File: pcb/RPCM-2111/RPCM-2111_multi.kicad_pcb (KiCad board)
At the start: 2 copper layers, 79.8 x 96.9 mm, 84 parts, among them J1 Conn_01x04_Female, J2 Conn_01x04_Female, J3 Conn_01x08_Female, J4 Conn_01x08_Female, J5 Conn_01x04_Female, J6 Conn_01x05_Female, J7 Conn_01x03_Female, J8 Conn_01x04_Female

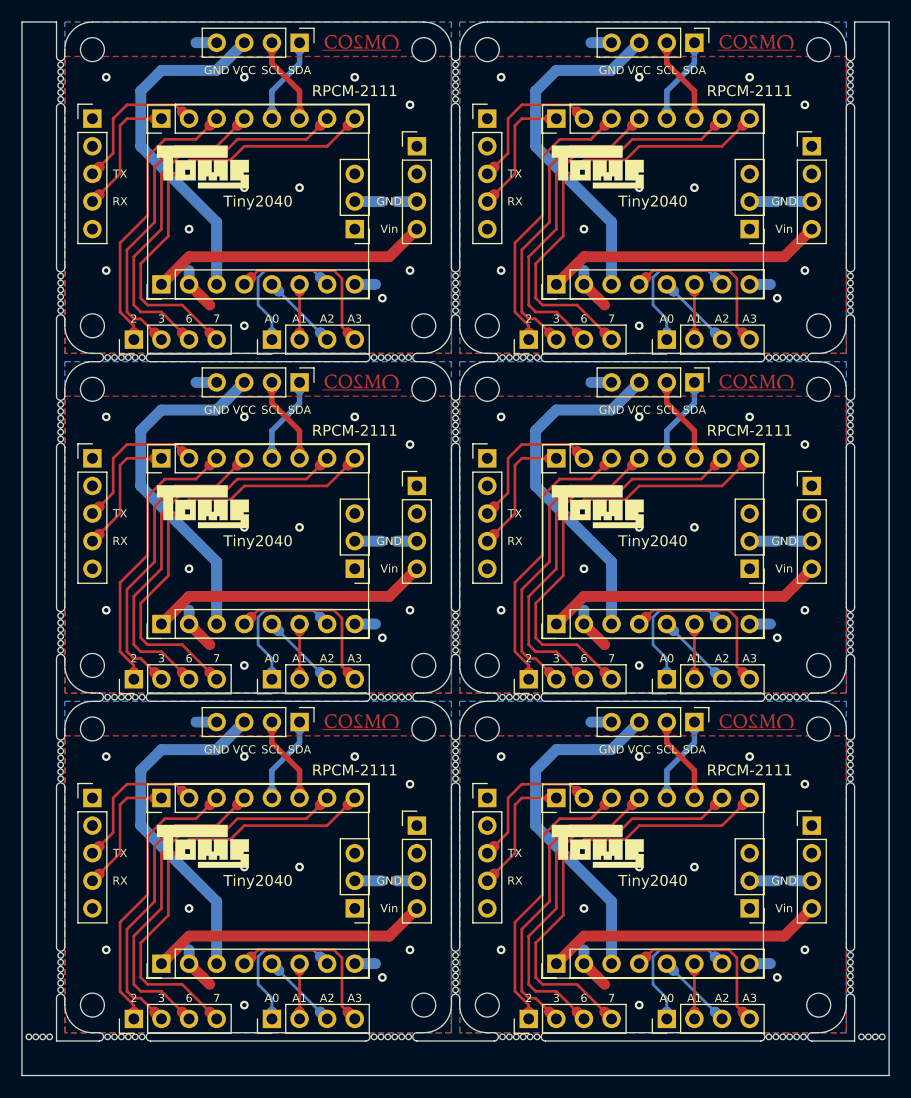
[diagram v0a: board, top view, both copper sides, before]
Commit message: :sparkles: fix to panelize
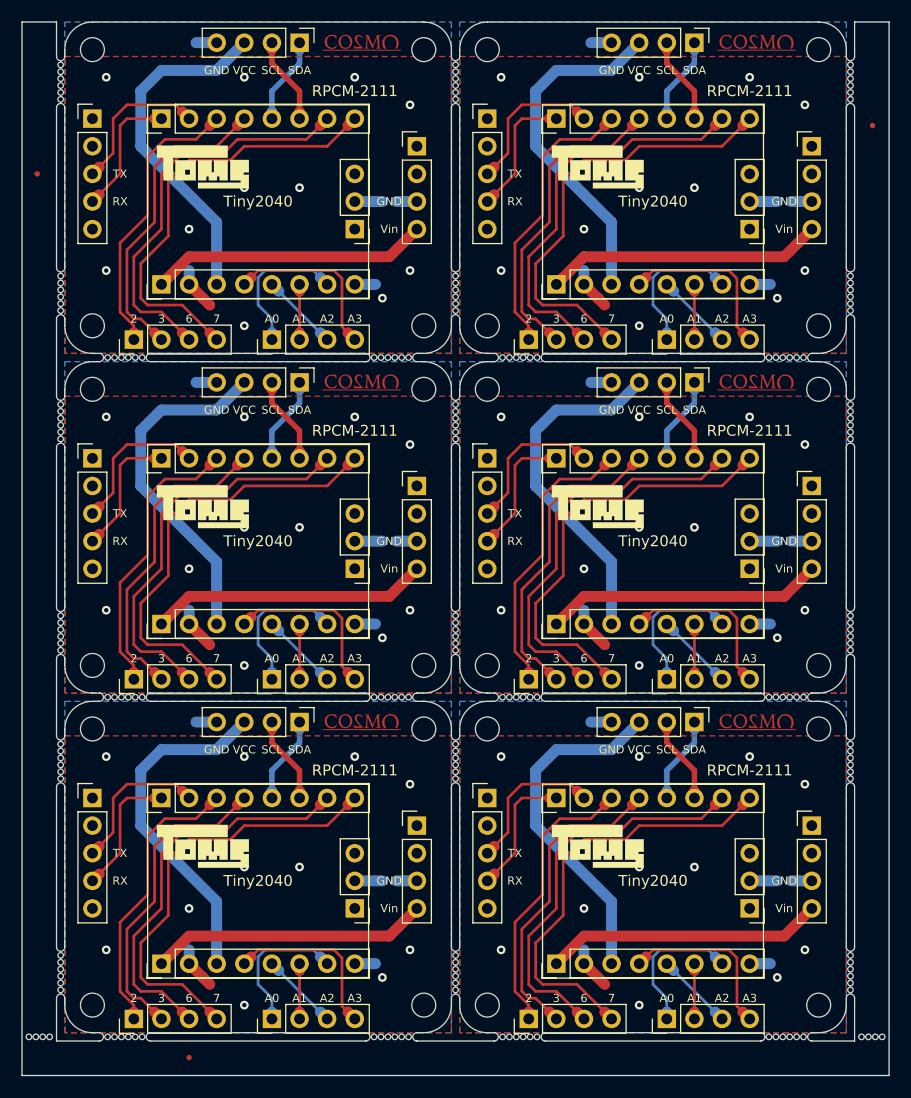
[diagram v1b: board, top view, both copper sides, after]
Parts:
- added REF**: Fiducial_0.5mm_Mask1mm, Fiducial:Fiducial_0.5mm_Mask1mm, F.Cu at (165.1, 61.6)
- added REF**: Fiducial_0.5mm_Mask1mm, Fiducial:Fiducial_0.5mm_Mask1mm, F.Cu at (102.2, 147.3)
- added REF**: Fiducial_0.5mm_Mask1mm, Fiducial:Fiducial_0.5mm_Mask1mm, F.Cu at (88.3, 66.0)
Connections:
- J3 pad 2: (no net) -> GND (x5)
- J3 pad 8: (no net) -> GND (x4)
- J5 pad 3: (no net) -> GND (x5)
- J7 pad 2: (no net) -> GND (x5)
- J8 pad 4: (no net) -> GND (x5)
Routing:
- net GND: track 12.2 -> 71.4 mm, vias 11 -> 66
- net (no net): track 1435.5 -> 1376.4 mm, vias 55 -> 0
- removed copper zone on B.Cu, net (none)
- removed copper zone on F.Cu, net (none)
